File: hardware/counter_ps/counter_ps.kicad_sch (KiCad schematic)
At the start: 18 parts, among them U1 LM317L_TO92, U2 LM337L_TO92

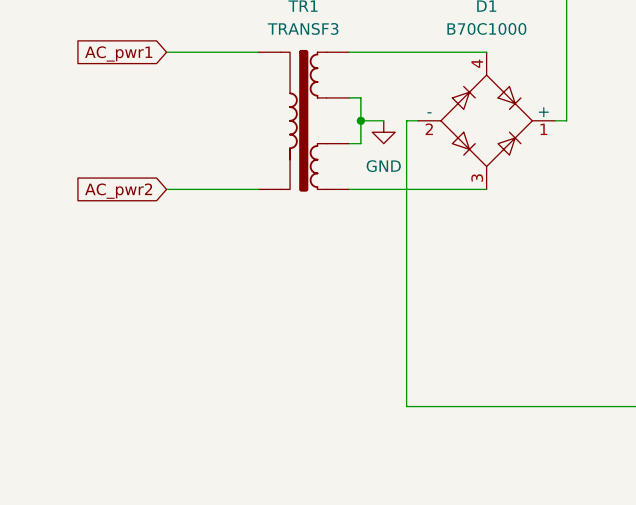
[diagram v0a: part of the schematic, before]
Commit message: mention transformer output current
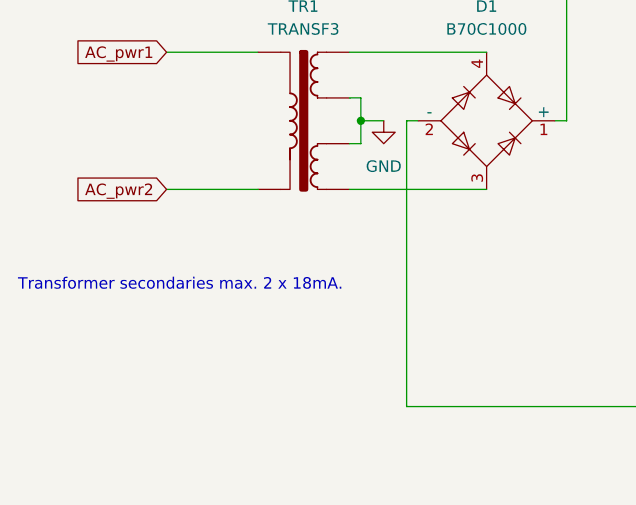
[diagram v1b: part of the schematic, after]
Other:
- note added: "Transformer secondaries max. 2 x 18mA."
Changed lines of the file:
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@@
     (stroke (width 0) (type default) (color 0 0 0 0))
+  )
+  (text "Transformer secondaries max. 2 x 18mA." (at 29.21 73.66 0)
+    (effects (font (size 1.27 1.27)) (justify left bottom))
   )
   (global_label "AC_pwr2" (shape input) (at 45.72 62.23 180) (fields_autoplaced)

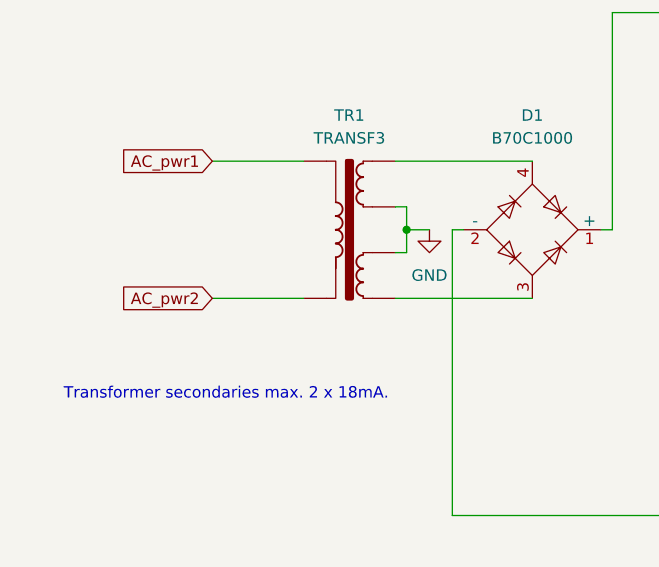
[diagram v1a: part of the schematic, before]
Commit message: transformer output voltage mentioned
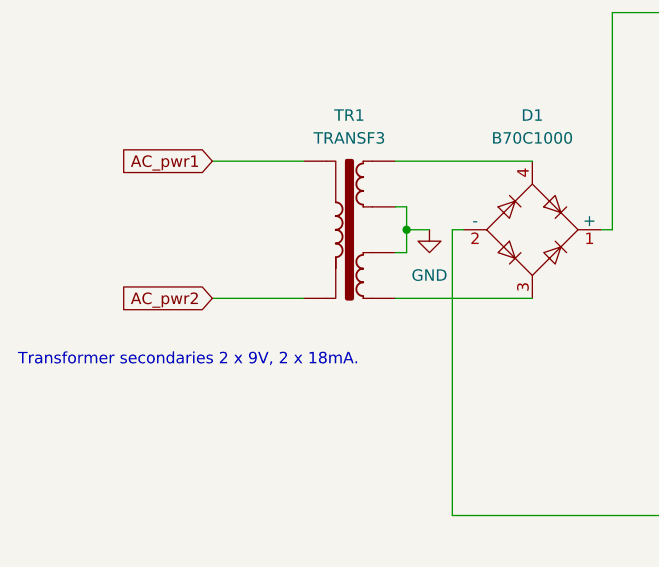
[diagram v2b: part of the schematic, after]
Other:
- note added: "Transformer secondaries 2 x 9V, 2 x 18mA."
- note removed: "Transformer secondaries max. 2 x 18mA."

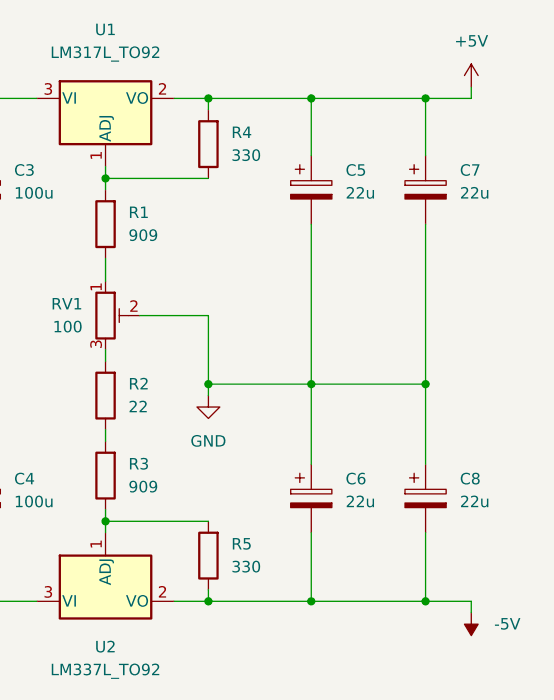
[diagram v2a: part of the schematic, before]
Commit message: 2nd 22u not needed
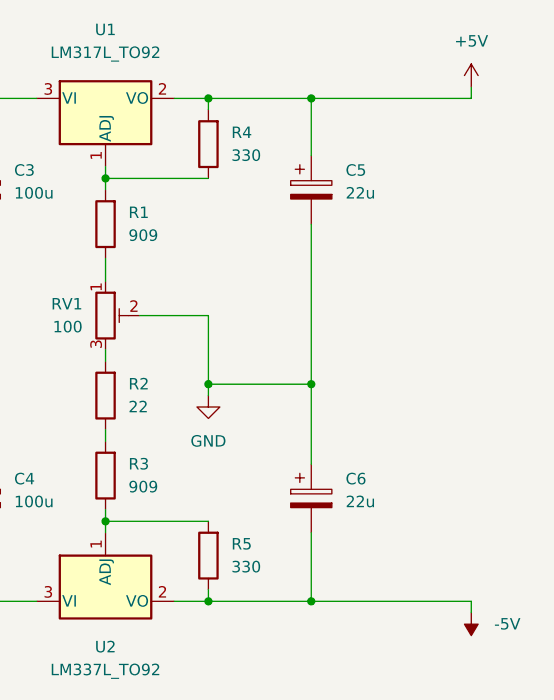
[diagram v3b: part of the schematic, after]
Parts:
- removed C7, C8: 22u, symbol Device:C_Polarized
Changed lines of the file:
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@@
   (junction (at 100.33 62.23) (diameter 0) (color 0 0 0 0)
   )
-  (junction (at 162.56 86.36) (diameter 0) (color 0 0 0 0)
-  )
   (junction (at 113.03 30.48) (diameter 0) (color 0 0 0 0)
   )
-  (junction (at 162.56 30.48) (diameter 0) (color 0 0 0 0)
-  )
-  (junction (at 162.56 62.23) (diameter 0) (color 0 0 0 0)
-  )
   (junction (at 149.86 86.36) (diameter 0) (color 0 0 0 0)
   )
@@
   (junction (at 149.86 62.23) (diameter 0) (color 0 0 0 0)
   )
-  (wire (pts (xy 149.86 86.36) (xy 162.56 86.36))
-    (stroke (width 0) (type default))
-  )
   (wire (pts (xy 90.17 30.48) (xy 100.33 30.48))
     (stroke (width 0) (type default))
@@
     (stroke (width 0) (type default))
   )
-  (wire (pts (xy 149.86 30.48) (xy 162.56 30.48))
+  (wire (pts (xy 149.86 30.48) (xy 167.64 30.48))
     (stroke (width 0) (type default))
   )
@@
     (stroke (width 0) (type default))
   )
-  (wire (pts (xy 162.56 62.23) (xy 162.56 71.12))
-    (stroke (width 0) (type default))
-  )
   (wire (pts (xy 66.04 62.23) (xy 81.28 62.23))
     (stroke (width 0) (type default))
@@
     (stroke (width 0) (type default))
   )
-  (wire (pts (xy 162.56 78.74) (xy 162.56 86.36))
-    (stroke (width 0) (type default))
-  )
   (wire (pts (xy 45.72 46.99) (xy 55.88 46.99))
     (stroke (width 0) (type default))
@@
     (stroke (width 0) (type default))
   )
-  (wire (pts (xy 149.86 62.23) (xy 162.56 62.23))
-    (stroke (width 0) (type default))
-  )
   (wire (pts (xy 100.33 30.48) (xy 100.33 36.83))
     (stroke (width 0) (type default))
@@
     (stroke (width 0) (type default))
   )
-  (wire (pts (xy 162.56 86.36) (xy 167.64 86.36))
+  (wire (pts (xy 149.86 86.36) (xy 167.64 86.36))
     (stroke (width 0) (type default))
   )
@@
     (stroke (width 0) (type default))
   )
-  (wire (pts (xy 162.56 30.48) (xy 162.56 36.83))
-    (stroke (width 0) (type default))
-  )
   (wire (pts (xy 113.03 30.48) (xy 113.03 36.83))
     (stroke (width 0) (type default))
@@
     (stroke (width 0) (type default))
   )
-  (wire (pts (xy 162.56 30.48) (xy 167.64 30.48))
-    (stroke (width 0) (type default))
-  )
   (wire (pts (xy 88.9 54.61) (xy 90.17 54.61))
     (stroke (width 0) (type default))
@@
   )
   (wire (pts (xy 138.43 62.23) (xy 149.86 62.23))
-    (stroke (width 0) (type default))
-  )
-  (wire (pts (xy 162.56 44.45) (xy 162.56 62.23))
     (stroke (width 0) (type default))
   )
@@
     )
   )
-  (symbol (lib_id "Device:C_Polarized") (at 162.56 74.93 0) (unit 1)
-    (in_bom yes) (on_board yes) (dnp no) (fields_autoplaced)
-    (property "Reference" "C8" (at 166.37 72.7709 0)
-      (effects (font (size 1.27 1.27)) (justify left))
-    )
-    (property "Value" "22u" (at 166.37 75.3109 0)
-      (effects (font (size 1.27 1.27)) (justify left))
-    )
-    (property "Footprint" "" (at 163.5252 78.74 0)
-      (effects (font (size 1.27 1.27)) hide)
-    )
-    (property "Datasheet" "~" (at 162.56 74.93 0)
-      (effects (font (size 1.27 1.27)) hide)
-    )
-    (pin "1")
-    (pin "2")
-    (instances
-      (project "counter_ps"
-        (path "/6e3a2f82-4214-4d3c-b586-5ac44c5a3fcf"
-          (reference "C8") (unit 1)
-        )
-      )
-    )
-  )
   (symbol (lib_id "Device:R") (at 127 44.45 180) (unit 1)
     (in_bom yes) (on_board yes) (dnp no) (fields_autoplaced)
@@
         )
       )
-    )
-  )
-  (symbol (lib_id "Device:C_Polarized") (at 162.56 40.64 0) (unit 1)
-    (in_bom yes) (on_board yes) (dnp no) (fields_autoplaced)
-    (property "Reference" "C7" (at 166.37 38.4809 0)
-      (effects (font (size 1.27 1.27)) (justify left))
-    )
-    (property "Value" "22u" (at 166.37 41.0209 0)
-      (effects (font (size 1.27 1.27)) (justify left))
-    )
-    (property "Footprint" "" (at 163.5252 44.45 0)
-      (effects (font (size 1.27 1.27)) hide)
-    )
-    (property "Datasheet" "~" (at 162.56 40.64 0)
-      (effects (font (size 1.27 1.27)) hide)
-    )
-    (pin "1")
-    (pin "2")
-    (instances
-      (project "counter_ps"
-        (path "/6e3a2f82-4214-4d3c-b586-5ac44c5a3fcf"
-          (reference "C7") (unit 1)
-        )
-      )
